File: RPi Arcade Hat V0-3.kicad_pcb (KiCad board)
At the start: 6 copper layers, 185.2 x 56.5 mm, 135 parts, among them J1 Raspberry_Pi_2_3, J10 Coin/Note Input, J11 +24V IN, J12 +12V OUT, J13 Player 1, J14 Player 2, J15 Player 3, J16 Player 4, J17 Counter Board, J18 HDSP-523E, J19 Coin Counter, J2 Player 1, J3 Player 2, J4 Player 3, J5 Player 4, J6 Spare, J7 +24V OUT, Q1 BC847, Q10 BC847, Q11 BC847, Q12 BC847, Q13 BC847, Q14 BC847, Q15 BC847, Q16 BC847, Q2 BC847, Q3 BC847, Q4 BC847, Q5 BC847, Q6 BC847, Q7 BC847, Q8 BC847, Q9 BC847, U1 SN74HC32N, U10 NE555DR, U12 SN74HC08N, U13 NE555DR, U14 SN74HC74N, U15 SN74HC32N, U16 SN74HC32N, U18 SN74HC08N, U3 LM2595S-12, U4 4510, U6 4510, U7 4511, U8 4511, U9 NE555DR

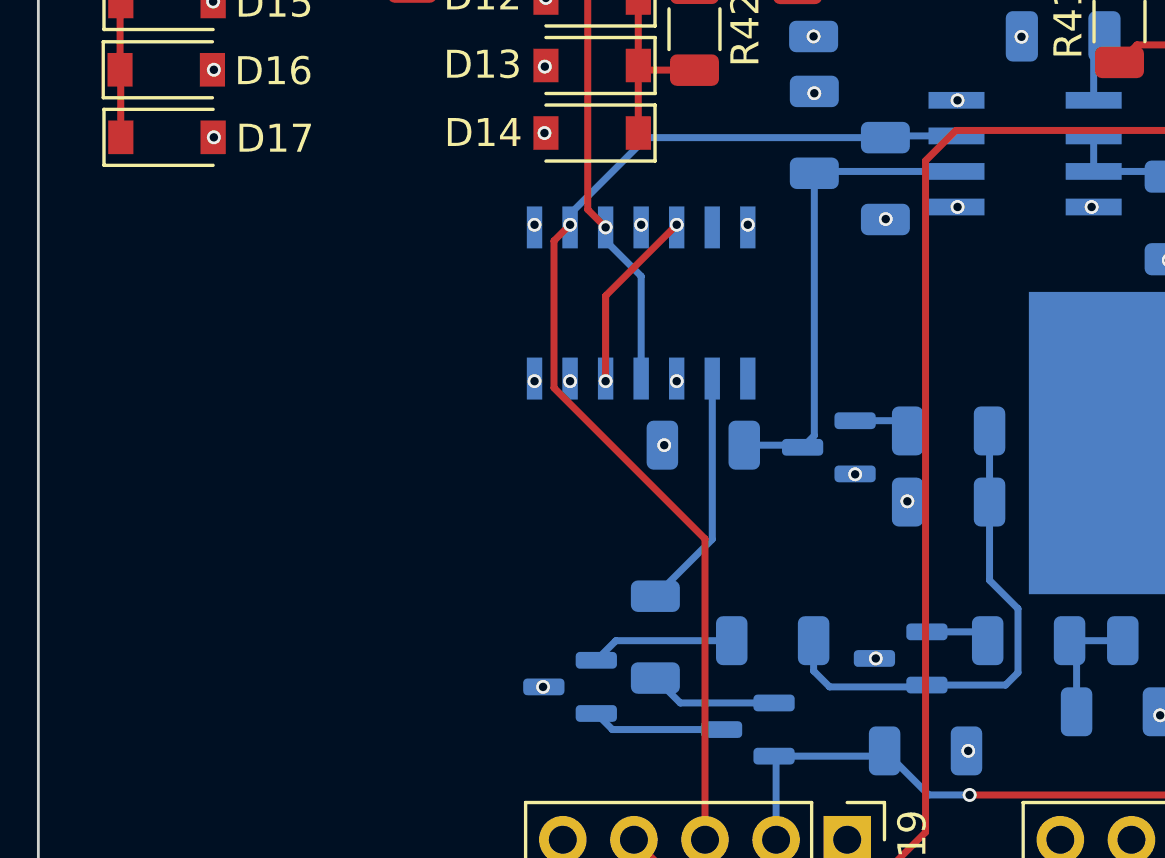
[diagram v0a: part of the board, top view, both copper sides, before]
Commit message: Error fixed
Found a wiring error in the circuit for the credit input, had it wired for NC logic (Active High), when should've been NO(Active Low)
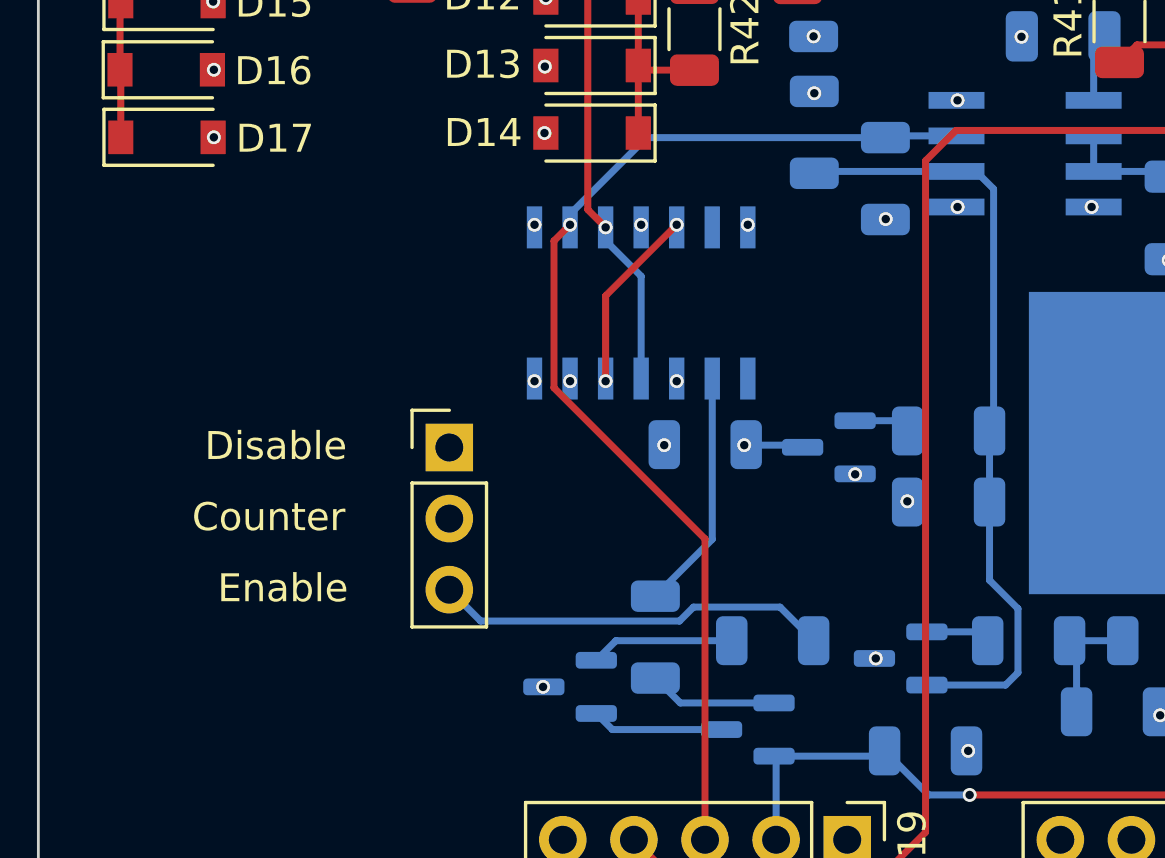
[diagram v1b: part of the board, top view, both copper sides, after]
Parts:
- added J8: Counter Bypass, Connector_PinHeader_2.54mm:PinHeader_1x03_P2.54mm_Vertical, F.Cu at (117.3, 104.9)
- moved R54 0.07 mm to (126.4, 104.7)
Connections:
- R35 pad 1: MECH (5V) NOT -> MECH (5V)
- R55 pad 1: MECH (5V) -> CNT PUL
- U10 pad 2: MECH (5V) NOT -> MECH (5V)
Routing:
- net P1CRDOUT: track 10.9 -> 77.5 mm
- net CNT PUL: track 0.00 -> 14.2 mm
- net MECH (5V): track 17.9 -> 28.0 mm
- net MECH (5V) NOT: track 17.2 -> 13.7 mm, vias 0 -> 1
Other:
- board text added: "Counter"
- board text added: "Disable"
- board text added: "Enable"

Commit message: PCB Redesigned as a Four Layer Board
I decided to redesign the PCB utilising screw terminals instead of IDC plugs, also made the PCB into a four layer board and Generated gerber's need to fix some silk screen details
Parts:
- added R52: 10k, Resistor_SMD:R_1206_3216Metric, F.Cu at (210.1, 111.0)
- C12, C13, C14, C15, C4, C5, D5, J17, L1, Q1, Q16, Q2, Q3, R1, R16, R17, R18, R21, R22, R23, R26, R28, R30, R32, R33, R35, R46, R47, R48, R49, R50, R51, R53, R54, R55, R56, R57, R8, R9, U1, U10, U12, U13, U14, U18, U3, U7, U8: moved to F.Cu
- J10, J11, J12, J18, J19, J7, J8: moved to B.Cu
- J13, J14, J15, J16: footprint Connector_PinHeader_2.54mm:PinHeader_1x02_P2.54mm_Vertical -> 2 Way Terminal Block:CONN-2X1_CTB0708&slash_2_CMD; moved to B.Cu
- J2, J3: footprint Connector_PinHeader_2.54mm:PinHeader_2x08_P2.54mm_Vertical -> 9Way Terminal:282836-9; moved to B.Cu
- J4: value Player 3 -> Spares; footprint Connector_PinHeader_2.54mm:PinHeader_2x08_P2.54mm_Vertical -> 9Way Terminal:282836-9; moved to B.Cu
- J5: value Player 4 -> Player 3; footprint Connector_PinHeader_2.54mm:PinHeader_2x08_P2.54mm_Vertical -> 9Way Terminal:282836-9; moved to B.Cu
- J6: value Spare -> Player 4; footprint Connector_PinHeader_2.54mm:PinHeader_2x08_P2.54mm_Vertical -> 9Way Terminal:282836-9; moved to B.Cu
- moved C15 148.8 mm to (275.0, 93.4), turned to -90 degrees
- moved U13 145.9 mm to (270.9, 94.8), turned to 0 degrees
- moved R48 140.6 mm to (273.3, 89.4), turned to 0 degrees
- moved R49 138.2 mm to (268.5, 89.4), turned to 0 degrees
- moved U14 136.2 mm to (260.1, 107.5), turned to 180 degrees
- moved J6 134.0 mm to (91.2, 78.3)
- moved C14 132.0 mm to (266.9, 96.3)
- moved R47 127.9 mm to (260.7, 99.3), turned to 0 degrees
- moved R35 125.7 mm to (255.9, 99.3), turned to 180 degrees
- moved C13 123.2 mm to (262.4, 92.9), turned to -90 degrees
- moved J5 121.6 mm to (91.2, 94.5)
- moved U10 120.4 mm to (258.3, 94.3), turned to 0 degrees
- moved U1 119.6 mm to (270.3, 107.5), turned to 0 degrees
- moved C12 117.9 mm to (260.7, 89.3), turned to 0 degrees
- moved Q16 117.3 mm to (248.8, 91.3), turned to 0 degrees
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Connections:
- J1 pad 11: Row 1 -> Row 4
- J1 pad 13: Row 2 -> Row 3
- J1 pad 15: Row 3 -> Row 2
- J1 pad 19: Row 4 -> Row 1
- J2 pad 1: Row 1 -> Column 1
- J2 pad 2: Column 1 -> Column 2
- J2 pad 3: Row 1 -> Column 3
- J2 pad 4: Column 2 -> Column 4
- J2 pad 5: Row 1 -> Column 5
- J2 pad 6: Column 3 -> Column 6
- J2 pad 7: Row 1 -> Column 7
- J2 pad 8: Column 4 -> Column 8
- J3 pad 1: Row 2 -> Column 1
- J3 pad 2: Column 1 -> Column 2
- J3 pad 3: Row 2 -> Column 3
- J3 pad 4: Column 2 -> Column 4
- J3 pad 5: Row 2 -> Column 5
- J3 pad 6: Column 3 -> Column 6
- J3 pad 7: Row 2 -> Column 7
- J3 pad 8: Column 4 -> Column 8
- J4 pad 1: Row 3 -> Column 8
- J4 pad 2: Column 1 -> Column 7
- J4 pad 3: Row 3 -> Column 6
- J4 pad 4: Column 2 -> Column 5
- J4 pad 5: Row 3 -> Column 4
- J4 pad 7: Row 3 -> Column 2
- J4 pad 8: Column 4 -> Column 1
- J4 pad 9: Row 3 -> Row 5
- J5 pad 1: Row 4 -> Column 1
- J5 pad 2: Column 1 -> Column 2
- J5 pad 3: Row 4 -> Column 3
- J5 pad 4: Column 2 -> Column 4
- J5 pad 5: Row 4 -> Column 5
- J5 pad 6: Column 3 -> Column 6
- J5 pad 7: Row 4 -> Column 7
- J5 pad 8: Column 4 -> Column 8
- J5 pad 9: Row 4 -> Row 3
- J6 pad 1: Row 5 -> Column 1
- J6 pad 2: Column 1 -> Column 2
- J6 pad 3: Row 5 -> Column 3
- J6 pad 4: Column 2 -> Column 4
- J6 pad 5: Row 5 -> Column 5
- J6 pad 6: Column 3 -> Column 6
- J6 pad 7: Row 5 -> Column 7
- J6 pad 8: Column 4 -> Column 8
- J6 pad 9: Row 5 -> Row 4
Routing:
- net Column 2: track 121.9 -> 287.3 mm, vias 1 -> 4
- net Column 1: track 67.2 -> 194.8 mm
- net Column 3: track 70.5 -> 194.2 mm
- net P4CRDBUTT: track 14.5 -> 134.2 mm
- net Column 5: track 72.3 -> 191.9 mm
- net Column 7: track 75.2 -> 194.0 mm
- net Column 4: track 76.0 -> 193.5 mm
- net Column 6: track 75.6 -> 191.4 mm
- net Column 8: track 80.8 -> 190.9 mm
- net Row 1: track 51.1 -> 159.0 mm, vias 0 -> 1
- net P3CRDBUTT: track 29.4 -> 119.1 mm, vias 1 -> 2
- net Row 2: track 54.4 -> 138.3 mm, vias 0 -> 1
- net GND: track 77.5 -> 0.00 mm, vias 27 -> 41
- net P2CRDBUTT: track 47.0 -> 109.9 mm, vias 3 -> 2
- net Row 3: track 63.6 -> 119.9 mm
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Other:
- board size 185.2 x 56.5 mm -> 240.9 x 64.4 mm
- copper layers 6 -> 4
- board text added: "1MHz Clock"
- board text added: "Credit Button"
- board text added: "Credit Timer"
- board text removed: "+12V Out"
- board text removed: "+24V In"
- board text removed: "+24V Out"
- board text removed: "C4"
- board text removed: "C5"
- board text removed: "Coin Counter"
- board text removed: "Coin/Credit Input"
- board text removed: "Counter"
- board text removed: "D5"
- board text removed: "L1"
- board text removed: "LM2595S-12"
- board text removed: "P1"
- board text removed: "P2"
- board text removed: "P3"
- board text removed: "P4"
- board text removed: "Spares"

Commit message: Minor Refinements, and Final Gerbers
Made some final refinements, and made sure that silkscreens were also correct before getting PCB's made
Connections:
- J1 pad 27: unconnected-(J1-Pad27) -> Column 9
- Q4 pad 3: Column 2 -> Column 9
- Q5 pad 3: Column 2 -> Column 9
- Q6 pad 3: Column 2 -> Column 9
- Q7 pad 3: Column 2 -> Column 9
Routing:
- net Column 2: track 287.3 -> 190.4 mm, vias 4 -> 0
- net Column 9: track 0.00 -> 76.8 mm, vias 0 -> 4
- net Column 8: track 190.9 -> 191.7 mm
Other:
- board size 240.9 x 64.4 mm -> 241.3 x 64.5 mm
- board text added: "+12V Out"
- board text added: "+24V In"
- board text added: "+24V Out"
- board text added: "1"
- board text added: "12V"
- board text added: "2"
- board text added: "3"
- board text added: "4"
- board text added: "5"
- board text added: "5V"
- board text added: "6"
- board text added: "7"
- board text added: "8"
- board text added: "Coin Pool Counter/Display"
- board text added: "Coin Pool Jumper"
- board text added: "Credit Buttons"
- board text added: "Credit Input"
- board text added: "GND"
- board text added: "Off"
- board text added: "On"
- board text added: "Signal GND"
- board text added: "Spares"
- board text removed: "Credit Button"
- board text removed: "Disable"
- board text removed: "Enable"
